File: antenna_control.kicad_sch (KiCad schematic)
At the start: 23 parts, among them J7 G125-MH11005L1P, J9 FTSH-105-01-L-DV-K, Q12 DMP2160UWQ-7, Q13 DMP3056LDM-7, U46 M0L1228QRGERQ1

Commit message: Minor comment updates
Signed-off-by: Corey Minyard <corey@minyard.net>
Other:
- note removed: "Optional pull up on the Extra ADC page."
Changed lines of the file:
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@@
-		)
-	)
-	(text "Optional pull up on\nthe Extra ADC page."
-		(exclude_from_sim no)
-		(at 202.184 93.472 0)
-		(effects
-			(font
-				(size 1.524 1.524)
-			)
 		)
 	)

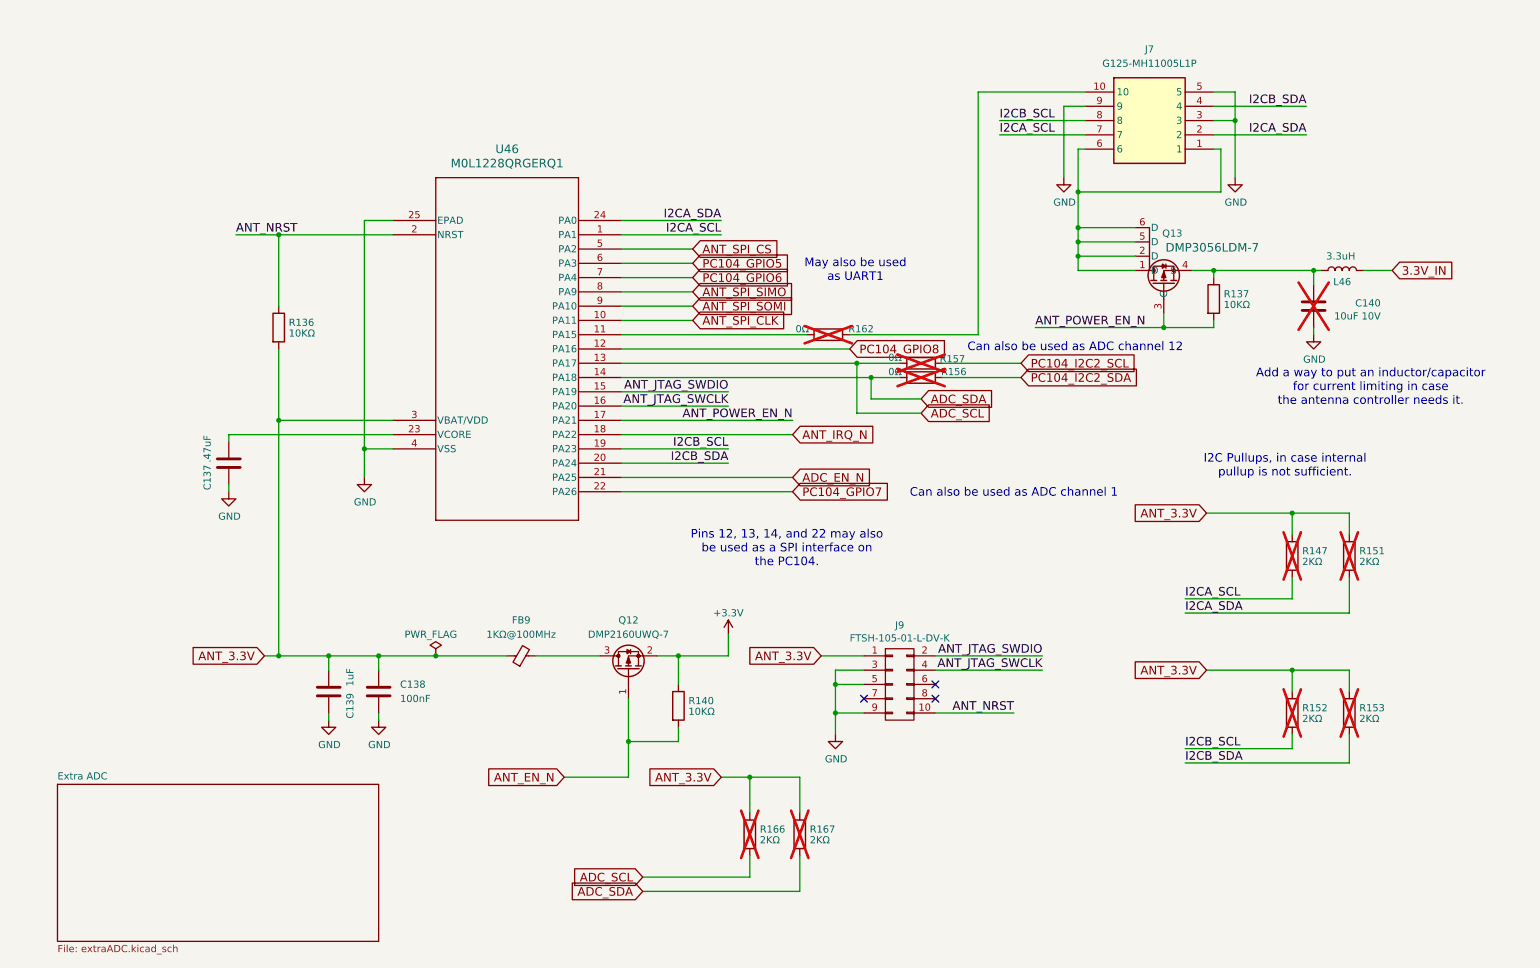
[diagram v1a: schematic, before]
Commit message: Rework the antenna controller I/Os
Allow the pins going to the PC104 to be used as a bootstrap loader
interface.

Signed-off-by: Corey Minyard <corey@minyard.net>
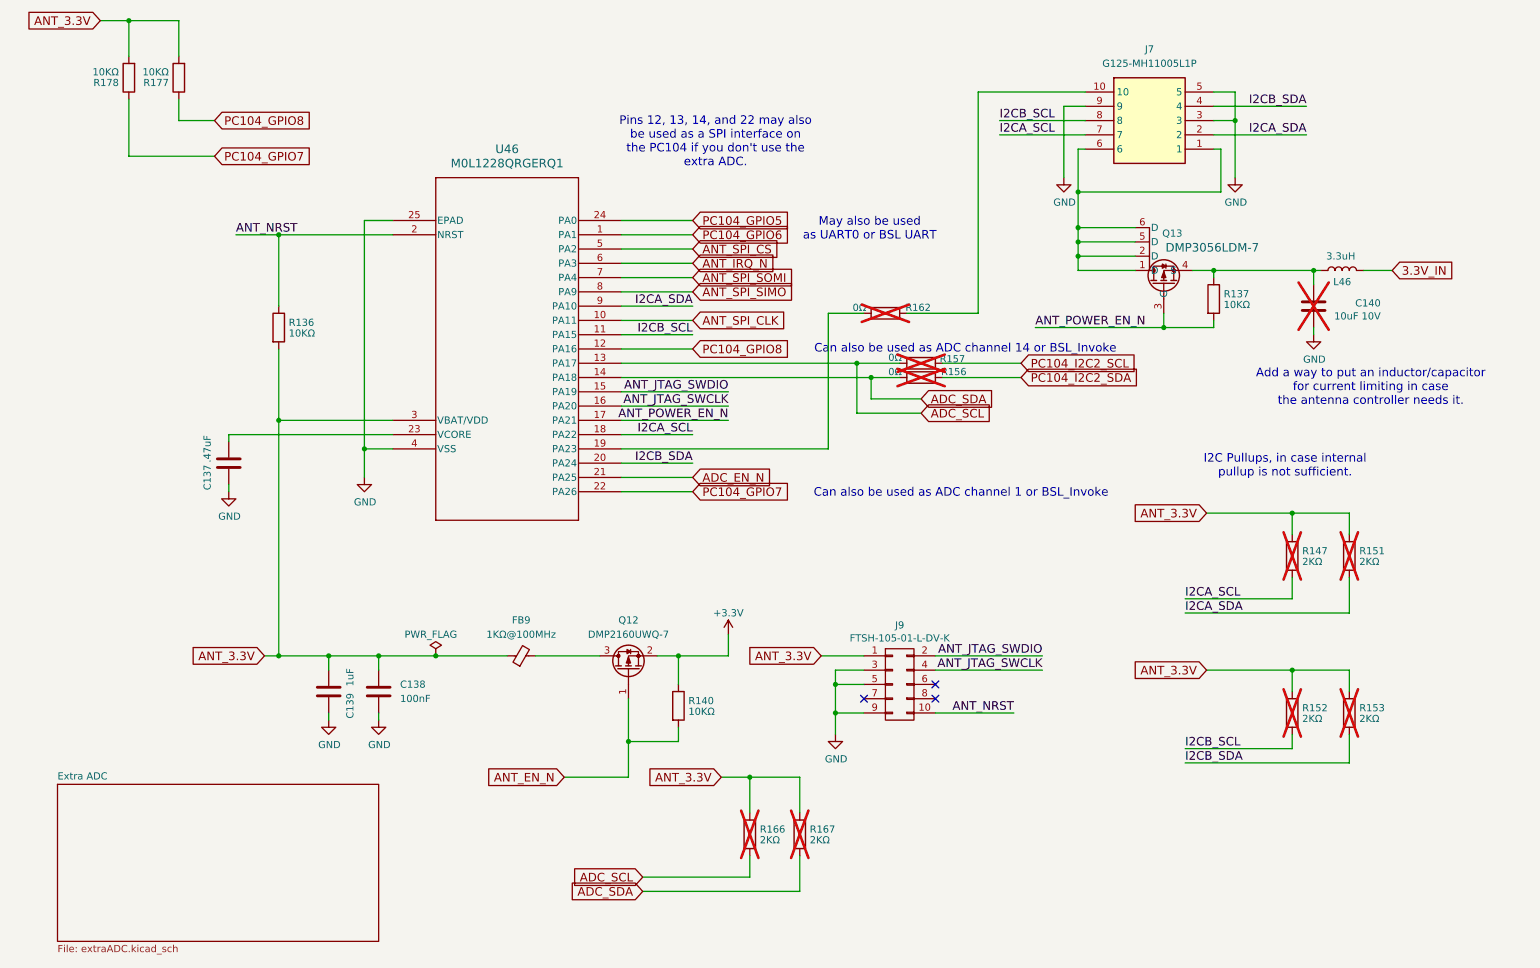
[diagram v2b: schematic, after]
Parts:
- added R177, R178: 10KΩ, Resistor_SMD:R_0402_1005Metric_Pad0.72x0.64mm_HandSolder, symbol Device:R
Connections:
- net ANT_3.3V: now also R177.2, R178.2
- net ANT_IRQ_N: now also U46.6 (PA3); no longer U46.18 (PA22)
- net ANT_SPI_SOMI: now also U46.7 (PA4); no longer U46.9 (PA10)
- net I2CA_SCL: now also U46.18 (PA22); no longer U46.1 (PA1)
- net I2CA_SDA: now also U46.9 (PA10); no longer U46.24 (PA0)
- net I2CB_SCL: now also U46.11 (PA15); no longer U46.19 (PA23)
- net PC104_GPIO5: now also U46.24 (PA0); no longer U46.6 (PA3)
- net PC104_GPIO6: now also U46.1 (PA1); no longer U46.7 (PA4)
- net PC104_GPIO7: now also R178.1
- net PC104_GPIO8: now also R177.1
- net at R162.2: now also U46.19 (PA23); no longer U46.11 (PA15)
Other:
- note added: "Can also be used as ADC channel 1 or BSL_Invoke"
- note added: "Can also be used as ADC channel 14 or BSL_Invoke"
- note added: "May also be used as UART0 or BSL UART"
- note added: "Pins 12, 13, 14, and 22 may also be used as a SPI interface on the PC104 if you don't use the extra ADC."
- note removed: "Can also be used as ADC channel 1"
- note removed: "Can also be used as ADC channel 12"
- note removed: "May also be used as UART1"
- note removed: "Pins 12, 13, 14, and 22 may also be used as a SPI interface on the PC104."
- moved on the sheet: R162

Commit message: Add a USB serial and power interface to the board
Signed-off-by: Corey Minyard <corey@minyard.net>
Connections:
- net PC104_GPIO5 renamed PC104_ACP_TX
- net PC104_GPIO6 renamed PC104_ACP_RX
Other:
- note removed: "May also be used as UART0 or BSL UART"
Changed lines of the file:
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@@
-		)
-	)
-	(text "May also be used\nas UART0 or BSL UART"
-		(exclude_from_sim no)
-		(at 168.656 61.214 0)
-		(effects
-			(font
-				(size 1.524 1.524)
-			)
 		)
 	)
@@
 		)
 	)
-	(global_label "PC104_GPIO6"
+	(global_label "PC104_ACP_RX"
 		(shape input)
 		(at 137.16 62.23 0)
@@
 		)
 		(property "Intersheetrefs" "${INTERSHEET_REFS}"
-			(at 155.3418 62.23 0)
+			(at 157.0109 62.23 0)
 			(effects
 				(font
@@
 		)
 	)
-	(global_label "PC104_GPIO5"
+	(global_label "PC104_ACP_TX"
 		(shape input)
 		(at 137.16 59.69 0)
@@
 		)
 		(property "Intersheetrefs" "${INTERSHEET_REFS}"
-			(at 155.3418 59.69 0)
+			(at 156.648 59.69 0)
 			(effects
 				(font

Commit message: Switch the USB power MOSFETs to a new part.
The other part had some issues, this is higher current, lower
resistance, lower leakage, and just better all around.

Signed-off-by: Corey Minyard <corey@minyard.net>
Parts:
- C140: now fitted; now in the parts list
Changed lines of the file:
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@@
 		(unit 1)
 		(exclude_from_sim no)
-		(in_bom no)
+		(in_bom yes)
 		(on_board yes)
-		(dnp yes)
+		(dnp no)
 		(property "Reference" "C140"
 			(at 259.588 74.3966 0)

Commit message: Change a capacitor value
Changed the 22uF caps to 22uF 16V.  Change the 10uF caps to 16V to
reflect what they really are.

Add some notes about some things.

Signed-off-by: Corey Minyard <corey@minyard.net>
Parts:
- C140: value 10uF 10V -> 10uF 16V
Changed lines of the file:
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@@
 			)
 		)
-		(property "Value" "10uF 10V"
+		(property "Value" "10uF 16V"
 			(at 259.588 76.708 0)
 			(effects

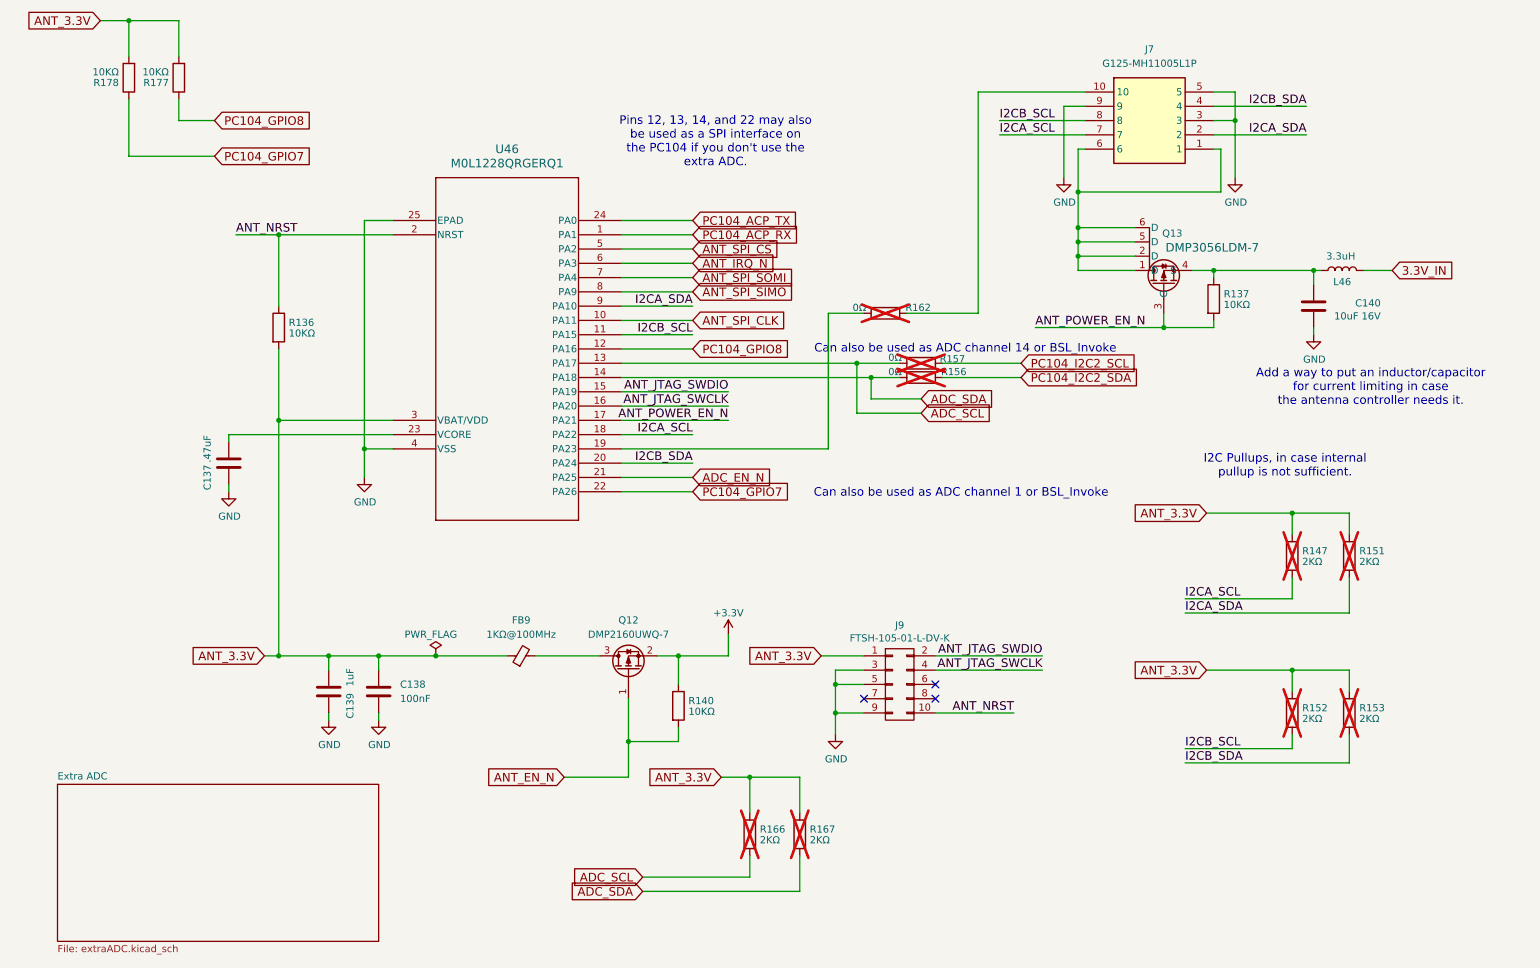
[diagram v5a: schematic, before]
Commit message: Fixes required from work on board version 3
Add a pullup to PC104\_ACP\_TX.  It's an open drain output, for some
strange reason doesn't have an internal pullup, and won't work right
without it.

Add 2.2K resistors for all the I2C pull ups.  You cannot use the
internal chip pull ups for this, it appears.

Add a line from the CPU DTR on the USB chip to turn on/off power to
the board from USB by driving the input of Q18.  I have verified that
DTR is high when not asserted and low when asserted, so it won't work
as-is, an inverter needs to be added between DTR and Q18.

Change the resistor R190 to 20K 1%.  The voltage is too high there, the
drop through the MOSFETs isn't as much as I expected.

Signed-off-by: Corey Minyard <corey@minyard.net>
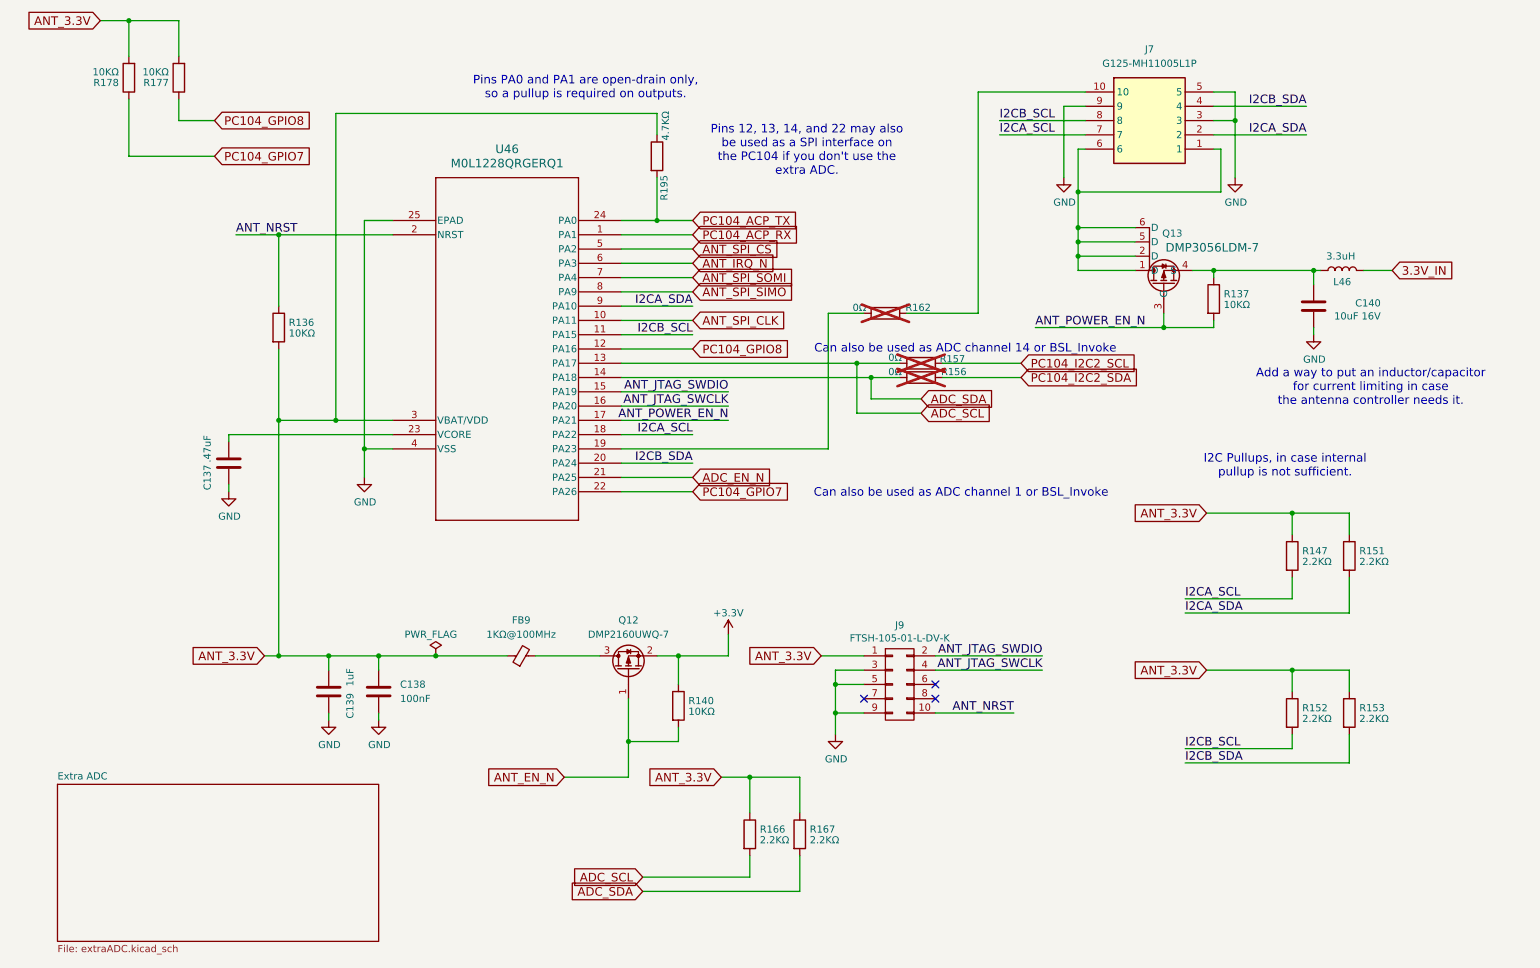
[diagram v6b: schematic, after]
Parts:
- added R195: 4.7KΩ, Resistor_SMD:R_0402_1005Metric_Pad0.72x0.64mm_HandSolder, symbol Device:R
- R147, R151, R152, R153, R166, R167: value 2KΩ -> 2.2KΩ; now fitted; now in the parts list
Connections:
- net ANT_3.3V: now also R195.1
- net PC104_ACP_TX: now also R195.2
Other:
- note added: "Pins PA0 and PA1 are open-drain only, so a pullup is required on outputs."
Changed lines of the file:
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@@
 		)
 	)
+	(text "Pins PA0 and PA1 are open-drain only,\nso a pullup is required on outputs."
+		(exclude_from_sim no)
+		(at 118.11 36.068 0)
+		(effects
+			(font
+				(size 1.524 1.524)
+			)
+		)
+	)
 	(text "I2C Pullups, in case internal\npullup is not sufficient."
 		(exclude_from_sim no)
@@
 	(text "Pins 12, 13, 14, and 22 may also\nbe used as a SPI interface on\nthe PC104 if you don't use the\nextra ADC."
 		(exclude_from_sim no)
-		(at 141.224 45.72 0)
+		(at 157.48 47.244 0)
 		(effects
 			(font
@@
 	)
 	(junction
+		(at 130.81 59.69)
+		(diameter 0)
+		(color 0 0 0 0)
+	)
+	(junction
 		(at 72.39 137.16)
 		(diameter 0)
@@
 		(color 0 0 0 0)
 	)
+	(junction
+		(at 73.66 95.25)
+		(diameter 0)
+		(color 0 0 0 0)
+	)
 	(no_connect
 		(at 167.64 144.78)
@@
 	(wire
 		(pts
-			(xy 124.46 59.69) (xy 137.16 59.69)
+			(xy 124.46 59.69) (xy 130.81 59.69)
+		)
+		(stroke
+			(width 0)
+			(type default)
+		)
+	)
+	(wire
+		(pts
+			(xy 130.81 40.64) (xy 73.66 40.64)
 		)
 		(stroke
@@
 	(wire
 		(pts
+			(xy 130.81 44.45) (xy 130.81 40.64)
+		)
+		(stroke
+			(width 0)
+			(type default)
+		)
+	)
+	(wire
+		(pts
 			(xy 124.46 74.93) (xy 137.16 74.93)
 		)
@@
 	(wire
 		(pts
-			(xy 63.5 95.25) (xy 83.82 95.25)
+			(xy 63.5 95.25) (xy 73.66 95.25)
 		)
 		(stroke
@@
 	(wire
 		(pts
+			(xy 130.81 52.07) (xy 130.81 59.69)
+		)
+		(stroke
+			(width 0)
+			(type default)
+		)
+	)
+	(wire
+		(pts
 			(xy 203.2 39.37) (xy 207.01 39.37)
 		)
@@
 	(wire
 		(pts
-			(xy 83.82 62.23) (xy 63.5 62.23)
+			(xy 63.5 62.23) (xy 83.82 62.23)
 		)
 		(stroke
@@
 	(wire
 		(pts
+			(xy 130.81 59.69) (xy 137.16 59.69)
+		)
+		(stroke
+			(width 0)
+			(type default)
+		)
+	)
+	(wire
+		(pts
 			(xy 229.87 36.83) (xy 233.68 36.83)
 		)
@@
 	(wire
 		(pts
+			(xy 73.66 95.25) (xy 83.82 95.25)
+		)
+		(stroke
+			(width 0)
+			(type default)
+		)
+	)
+	(wire
+		(pts
 			(xy 147.32 158.75) (xy 147.32 165.1)
 		)
@@
 	(wire
 		(pts
+			(xy 73.66 40.64) (xy 73.66 95.25)
+		)
+		(stroke
+			(width 0)
+			(type default)
+		)
+	)
+	(wire
+		(pts
 			(xy 228.6 111.76) (xy 243.84 111.76)
 		)
@@
 		(unit 1)
 		(exclude_from_sim no)
-		(in_bom no)
+		(in_bom yes)
 		(on_board yes)
-		(dnp yes)
+		(dnp no)
 		(property "Reference" "R151"
 			(at 255.778 118.491 0)
@@
 			)
 		)
-		(property "Value" "2KΩ"
+		(property "Value" "2.2KΩ"
 			(at 255.778 120.396 0)
 			(effects
@@
 		(unit 1)
 		(exclude_from_sim no)
-		(in_bom no)
+		(in_bom yes)
 		(on_board yes)
-		(dnp yes)
+		(dnp no)
 		(property "Reference" "R166"
 			(at 149.098 168.021 0)
@@
 			)
 		)
-		(property "Value" "2KΩ"
+		(property "Value" "2.2KΩ"
 			(at 149.098 169.926 0)
 			(effects
@@
 		(unit 1)
 		(exclude_from_sim no)
-		(in_bom no)
+		(in_bom yes)
 		(on_board yes)
-		(dnp yes)
+		(dnp no)
 		(property "Reference" "R153"
 			(at 255.778 146.431 0)
@@
 			)
 		)
-		(property "Value" "2KΩ"
+		(property "Value" "2.2KΩ"
 			(at 255.778 148.336 0)
 			(effects
@@
 	)
 	(symbol
+		(lib_id "Device:R")
+		(at 130.81 48.26 0)
+		(unit 1)
+		(exclude_from_sim no)
+		(in_bom yes)
+		(on_board yes)
+		(dnp no)
+		(property "Reference" "R195"
+			(at 132.08 56.134 90)
+			(effects
+				(font
+					(size 1.27 1.27)
+				)
+				(justify left)
+			)
+		)
+		(property "Value" "4.7KΩ"
+			(at 132.334 45.466 90)
+			(effects
+				(font
+					(size 1.27 1.27)
+				)
+				(justify left)
+			)
+		)
+		(property "Footprint" "Resistor_SMD:R_0402_1005Metric_Pad0.72x0.64mm_HandSolder"
+			(at 129.032 48.26 90)
+			(effects
+				(font
+					(size 1.27 1.27)
+				)
+				(hide yes)
+			)
+		)
+		(property "Datasheet" "~"
+			(at 130.81 48.26 0)
+			(effects
+				(font
+					(size 1.27 1.27)
+				)
+			)
+		)
+		(property "Description" ""
+			(at 130.81 48.26 0)
+			(effects
+				(font
+					(size 1.27 1.27)
+				)
+			)
+		)
+		(pin "1"
+		)
+		(pin "2"
+		)
+		(instances
+			(project "PacSat_AFSK"
+				(path "/cc9f42d2-6985-41ac-acab-5ab7b01c5b38/75b01062-9747-4556-85bc-485f2c3c99d3"
+					(reference "R195")
+					(unit 1)
+				)
+			)
+		)
+	)
+	(symbol
 		(lib_id "power:PWR_FLAG")
 		(at 91.44 137.16 0)
@@
 		(unit 1)
 		(exclude_from_sim no)
-		(in_bom no)
+		(in_bom yes)
 		(on_board yes)
-		(dnp yes)
+		(dnp no)
 		(property "Reference" "R147"
 			(at 245.618 118.491 0)
@@
 			)
 		)
-		(property "Value" "2KΩ"
+		(property "Value" "2.2KΩ"
 			(at 245.618 120.396 0)
 			(effects
@@
 		(unit 1)
 		(exclude_from_sim no)
-		(in_bom no)
+		(in_bom yes)
 		(on_board yes)
-		(dnp yes)
+		(dnp no)
 		(property "Reference" "R152"
 			(at 245.618 146.431 0)
@@
 			)
 		)
-		(property "Value" "2KΩ"
+		(property "Value" "2.2KΩ"
 			(at 245.618 148.336 0)
 			(effects
@@
 		(unit 1)
 		(exclude_from_sim no)
-		(in_bom no)
+		(in_bom yes)
 		(on_board yes)
-		(dnp yes)
+		(dnp no)
 		(property "Reference" "R167"
 			(at 157.988 168.021 0)
@@
 			)
 		)
-		(property "Value" "2KΩ"
+		(property "Value" "2.2KΩ"
 			(at 157.988 169.926 0)
 			(effects
